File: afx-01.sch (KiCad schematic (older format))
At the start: 10 parts, among them P1 CONN_02X05, P2 CONN_02X05, U1 ADA_SSD1306_I2C, U2 Teensy_3.1, U4 MicroSD_Adapter, U5 SSD1306

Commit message: BIG UPDATE! omg so big
New boards and other things.. jeesh it sbeen too long since the last update
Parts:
- removed P2: CONN_02X05, ab2_header:AB2_HDR_M05-2V, symbol CONN_02X05
- removed U5: SSD1306, afx-01:SSD1306_XL, symbol SSD1306
- added P?: CONN_02X05, ab2_header:AB2_HDR_M05-2V, symbol CONN_02X05
- added U?: MCP1703, symbol MCP1703
- U1: footprint afx-01:SSD1306 -> Zetaohm:SSD1306
- U2: footprint afx-01:Teensy3.1 -> Zetaohm:Teensy3.1
- U4: footprint afx-01:MicroSD -> Zetaohm:MicroSD
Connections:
- net labels added: +3V3, +5V, CV_IN1, CV_IN2, CV_IN3, CV_IN4, DAC_CS, DAC_SDO, DISP_RESET, ENC1A, ENC1B, ENC2A, ENC2B, GATE_IN1, GATE_IN2, GATE_IN3, GATE_IN4, GNDA, LED_DIN, MIDI_IN_EXTERNAL, MIDI_OUT_EXTERNAL, MIDI_OUT_INTERNAL, MISO, MOSI, SCL0, SCL1, SCLK, SDA0, SDA1, SD_CS, SPARE_ANALOG1, VDD, VSS
- net labels removed: 10, 11, 12, 13, 15, 20, 22, 24, 25, 26, 29, 3, 30, 4, 5, 6, 9, AGND, VCC, VIN
- wire segments 110 -> 122
- no-connect marks 22 -> 19
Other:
- note added: "5V VOLTAGE REGULATOR"
- note added: "AUX CONNECTOR"
- note added: "EXTERNAL POWER BUS"
- note added: "I2C PULLUP RESISTORS"
- note added: "ZETAOHM AFX-01"
- moved on the sheet: P1, R16, R17, R18, R19, U1, U2, U4

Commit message: UPDATEUPDATES!!!
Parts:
- removed P?: CONN_02X05, ab2_header:AB2_HDR_M05-2V, symbol CONN_02X05
- added JP1, JP2, JP3: JUMPER3, Zetaohm:Jumper_3way, symbol JUMPER3
- added P2: CONN_02X08, Pin_Headers:Pin_Header_Angled_2x08, symbol CONN_02X08
- added Q5, Q6: BSS138, Housings_SOT-23_SOT-143_TSOT-6:SOT-23, symbol BSS138
- added R72, R73: 4.7k, Resistors_SMD:R_0805_HandSoldering, symbol Resistor
- added U?: MicroSD_Connector, Zetaohm:AMPHENOL_MICROSD, symbol MicroSD_Connector
- U2: footprint Zetaohm:Teensy3.1 -> Zetaohm:Teensy3.1_Min_I2C2
- U5: renamed from U?; footprint (none) -> Housings_SOT-23_SOT-143_TSOT-6:SOT-23_Handsoldering
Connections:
- net +3V3: now also Q5.1 (G), U?.4 (VDD)
- net +5V: now also JP3.2, R72.2, R73.2; no longer U5.2 (VOUT)
- net GND: now also P2.3 (P3), P2.4 (P4), P2.5 (P5), P2.6 (P6), P2.7 (P7), P2.8 (P8), U?.6 (VSS)
- net MISO: now also U?.7 (MISO)
- net MOSI: now also U?.3 (MOSI)
- net SCL0: now also JP2.1, Q6.2 (S)
- net SCL1: now also JP2.3; no longer U1.2 (SCL)
- net SCLK: now also U?.5 (SCLK)
- net SDA0: now also JP1.1, Q5.2 (S)
- net SDA1: now also JP1.3; no longer U1.1 (SDA)
- net SD_CS: now also U?.2 (CS)
- net VDD: now also P2.1 (P1), P2.2 (P2)
- net VSS: now also P2.10 (P10), P2.9 (P9)
- new net: JP1.2, U1.1 (SDA)
- new net: JP2.2, U1.2 (SCL)
- new net: JP3.1, U5.2 (VOUT)
- new net: JP3.3, P2.11 (P11), P2.12 (P12)
- new net SCL0_5v: Q5.3 (D), R72.1
- new net SDA0_5v: Q6.3 (D), R73.1
- no-connect marks 19 -> 25
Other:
- note added: "5V SOURCE\nSELECTOR"
- note added: "I2C PULLUP RESISTORS + LOGIC LEVEL SHIFTER"
- note removed: "I2C PULLUP RESISTORS"
- moved on the sheet: P1, R16, R17, R18, R19, U1, U2, U4, U5

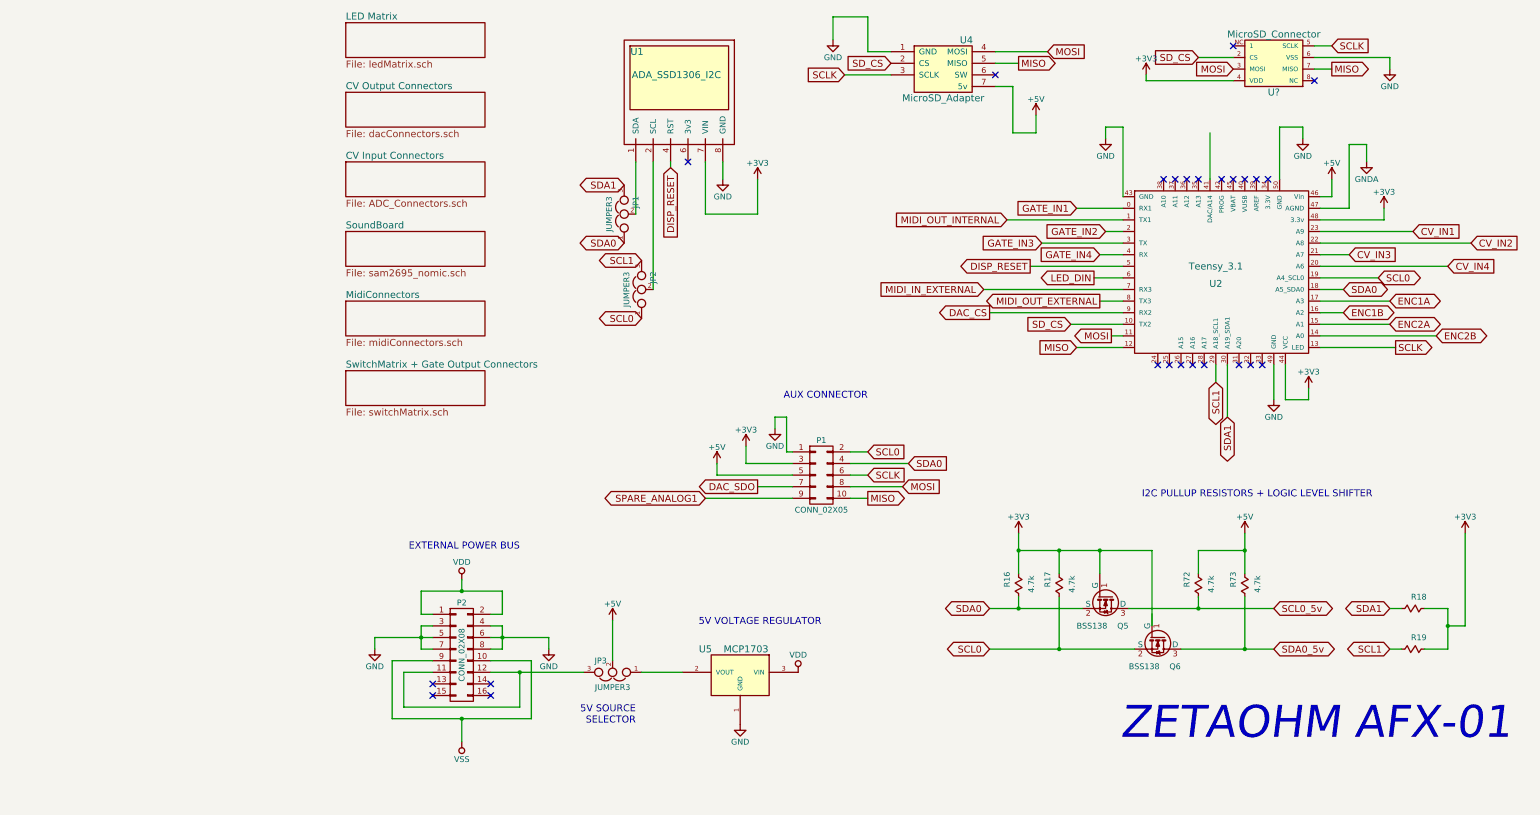
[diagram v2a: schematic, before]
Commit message: Added Touch Capacitive Panel
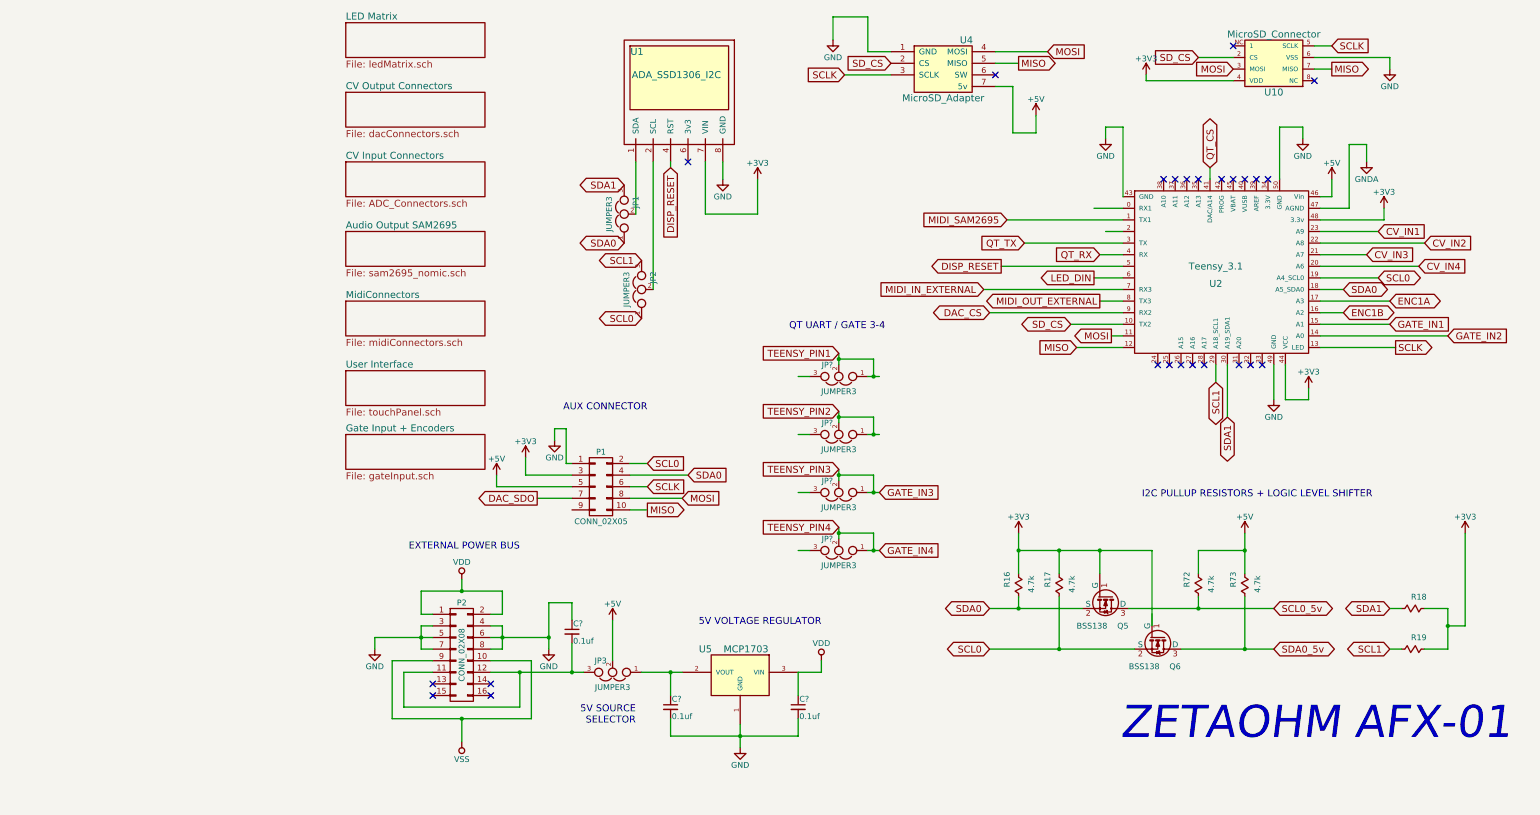
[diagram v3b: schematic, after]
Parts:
- added C? (x3): 0.1uf, symbol C_Small
- added JP? (x4): JUMPER3, Zetaohm:Jumper_3way, symbol JUMPER3
- gave numbers to parts that had none: 1
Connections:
- net labels added: MIDI_SAM2695, QT_CS, QT_RX, QT_TX, TEENSY_PIN1, TEENSY_PIN2, TEENSY_PIN3, TEENSY_PIN4
- net labels removed: ENC2A, ENC2B, MIDI_OUT_INTERNAL, SPARE_ANALOG1
- wire segments 138 -> 197
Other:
- note added: "QT UART / GATE 3-4"
- moved on the sheet: P1

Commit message: Updating Schematics
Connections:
- wire segments 197 -> 168
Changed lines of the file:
@@
 	3800 2000 3800 2050
 Wire Wire Line
-	6800 5200 6800 5350
-Wire Wire Line
-	6800 5350 6800 5550
-Wire Wire Line
-	6800 5350 7150 5350
-Wire Wire Line
-	7150 5350 7500 5350
-Wire Wire Line
-	7500 5350 7950 5350
+	6800 5200 6800 5550
+Wire Wire Line
+	6800 5350 7950 5350
 Wire Wire Line
 	7150 5350 7150 5550
@@
 	10300 5850 10500 5850
 Wire Wire Line
-	10500 5850 10500 6000
-Wire Wire Line
-	10500 6000 10500 6200
+	10500 5850 10500 6200
 Wire Wire Line
 	10500 6200 10300 6200
@@
 	1650 5900 1650 5700
 Wire Wire Line
-	1650 5700 2000 5700
-Wire Wire Line
-	2000 5700 2350 5700
+	1650 5700 2350 5700
 Wire Wire Line
 	2350 5700 2350 5900
@@
 	1400 6300 1400 6800
 Wire Wire Line
-	1400 6800 2000 6800
-Wire Wire Line
-	2000 6800 2600 6800
+	1400 6800 2600 6800
 Wire Wire Line
 	2600 6800 2600 6300
@@
 	1750 6000 1650 6000
 Wire Wire Line
-	1650 6000 1650 6100
-Wire Wire Line
-	1650 6100 1650 6200
+	1650 6000 1650 6200
 Wire Wire Line
 	1650 6200 1750 6200
 Wire Wire Line
-	1250 6100 1650 6100
-Wire Wire Line
-	1650 6100 1750 6100
+	1250 6100 1750 6100
 Connection ~ 1650 6100
 Wire Wire Line
@@
 	2350 6200 2250 6200
 Wire Wire Line
-	2350 6000 2350 6100
-Wire Wire Line
-	2350 6100 2350 6200
+	2350 6000 2350 6200
 Wire Wire Line
 	2350 6000 2250 6000
 Wire Wire Line
-	2250 6100 2350 6100
-Wire Wire Line
-	2350 6100 2750 6100
+	2250 6100 2750 6100
 Connection ~ 2350 6100
 Wire Wire Line
@@
 	7700 3000 7450 3000
 Wire Wire Line
-	2750 5800 2750 6100
-Wire Wire Line
-	2750 6100 2750 6200
+	2750 5800 2750 6200
 Wire Wire Line
 	7700 3300 6550 3300
@@
 	8450 2050 8450 2150
 Wire Wire Line
-	6550 5850 6800 5850
-Wire Wire Line
-	6800 5850 7350 5850
-Wire Wire Line
-	6550 6200 7150 6200
-Wire Wire Line
-	7150 6200 7800 6200
+	6550 5850 7350 5850
+Wire Wire Line
+	6550 6200 7800 6200
 Connection ~ 7150 6200
 Connection ~ 6800 5850
@@
 Connection ~ 7500 5350
 Wire Wire Line
-	7750 5850 8350 5850
-Wire Wire Line
-	8350 5850 9000 5850
-Wire Wire Line
-	8200 6200 8750 6200
-Wire Wire Line
-	8750 6200 9000 6200
+	7750 5850 9000 5850
+Wire Wire Line
+	8200 6200 9000 6200
 Wire Wire Line
 	8350 5750 8350 5850
@@
 	8350 5350 8750 5350
 Wire Wire Line
-	8750 5200 8750 5350
-Wire Wire Line
-	8750 5350 8750 5550
+	8750 5200 8750 5550
 Connection ~ 8750 5350
 Wire Wire Line
-	2250 6400 2500 6400
-Wire Wire Line
-	2500 6400 2950 6400
-Wire Wire Line
-	2950 6400 3050 6400
-Wire Wire Line
-	3550 6400 3800 6400
-Wire Wire Line
-	3800 6400 3900 6400
+	2250 6400 3050 6400
+Wire Wire Line
+	3550 6400 3900 6400
 Wire Wire Line
 	3300 6300 3300 5950
@@
 	3800 6800 3800 6950
 Wire Wire Line
-	3800 6950 4400 6950
-Wire Wire Line
-	4400 6950 4900 6950
-Wire Wire Line
-	4400 6850 4400 6950
-Wire Wire Line
-	4400 6950 4400 7050
+	3800 6950 4900 6950
+Wire Wire Line
+	4400 6850 4400 7050
 Connection ~ 4400 6950
 Wire Wire Line
@@
 	4900 4850 5000 4850
 Wire Wire Line
-	5250 4650 5250 4700
-Wire Wire Line
-	5250 4700 5250 4750
-Wire Wire Line
-	5500 4850 5550 4850
-Wire Wire Line
-	5550 4850 5600 4850
-Wire Wire Line
-	5600 5350 5550 5350
-Wire Wire Line
-	5550 5350 5500 5350
+	5250 4650 5250 4750
+Wire Wire Line
+	5500 4850 5600 4850
+Wire Wire Line
+	5500 5350 5600 5350
 Wire Wire Line
 	5000 5350 4900 5350
 Wire Wire Line
-	5250 5250 5250 5200
-Wire Wire Line
-	5250 5200 5250 5150
+	5250 5150 5250 5250
 Wire Wire Line
 	4900 3850 5000 3850
 Wire Wire Line
-	5250 3650 5250 3700
-Wire Wire Line
-	5250 3700 5250 3750
-Wire Wire Line
-	5500 3850 5550 3850
-Wire Wire Line
-	5550 3850 5600 3850
-Wire Wire Line
-	5600 4350 5550 4350
-Wire Wire Line
-	5550 4350 5500 4350
+	5250 3650 5250 3750
+Wire Wire Line
+	5500 3850 5600 3850
+Wire Wire Line
+	5500 4350 5600 4350
 Wire Wire Line
 	5000 4350 4900 4350
 Wire Wire Line
-	5250 4250 5250 4200
-Wire Wire Line
-	5250 4200 5250 4150
+	5250 4150 5250 4250
 Wire Wire Line
 	5250 3700 5550 3700
